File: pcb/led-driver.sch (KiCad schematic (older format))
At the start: 33 parts, among them Q201 Q_NMOS_GDSD, Q202 Q_NMOS_GDSD, Q203 Q_NMOS_GDSD, Q204 Q_NMOS_GDSD, Q205 NPN, Q206 NPN, Q207 NPN, Q208 NPN, U201 LM2902N, U202 MAX5813

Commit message: removed resistor dividors, added cap to usb
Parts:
- removed R205, R206, R207, R208, R209, R210, R211, R212: 10k, netl:SMD_0603, symbol R
- R213, R214, R215, R216, R217, R218, R219, R220: footprint (none) -> netl:SMD_0603
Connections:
- net A: now also U201.3 (+)
- net B: now also U201.5 (+)
- net C: now also U201.10 (+)
- net D: now also U201.12 (+)

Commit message: added mcu
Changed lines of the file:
@@
 $EndComp
 $Comp
-L GND #PWR026
+L GND #PWR022
 U 1 1 56C32C0C
 P 6350 4850
-F 0 "#PWR026" H 6350 4600 50  0001 C CNN
+F 0 "#PWR022" H 6350 4600 50  0001 C CNN
 F 1 "GND" H 6350 4700 50  0000 C CNN
 F 2 "" H 6350 4850 60  0000 C CNN
@@
 $EndComp
 $Comp
-L GND #PWR027
+L GND #PWR023
 U 1 1 56C32E31
 P 3200 4850
-F 0 "#PWR027" H 3200 4600 50  0001 C CNN
+F 0 "#PWR023" H 3200 4600 50  0001 C CNN
 F 1 "GND" H 3200 4700 50  0000 C CNN
 F 2 "" H 3200 4850 60  0000 C CNN
@@
 $EndComp
 $Comp
-L GND #PWR028
+L GND #PWR024
 U 1 1 56C32F90
 P 3200 2550
-F 0 "#PWR028" H 3200 2300 50  0001 C CNN
+F 0 "#PWR024" H 3200 2300 50  0001 C CNN
 F 1 "GND" H 3200 2400 50  0000 C CNN
 F 2 "" H 3200 2550 60  0000 C CNN
@@
 $EndComp
 $Comp
-L GND #PWR029
+L GND #PWR025
 U 1 1 56C33072
 P 6350 2550
-F 0 "#PWR029" H 6350 2300 50  0001 C CNN
+F 0 "#PWR025" H 6350 2300 50  0001 C CNN
 F 1 "GND" H 6350 2400 50  0000 C CNN
 F 2 "" H 6350 2550 60  0000 C CNN
@@
 	3550 2450 3550 2550
 Wire Wire Line
-	3550 1900 3550 2050
-Wire Wire Line
-	3550 2050 3550 2150
+	3550 1900 3550 2150
 Wire Wire Line
 	2200 1000 2200 1300
@@
 Connection ~ 6700 2050
 Wire Wire Line
-	6700 1900 6700 2050
-Wire Wire Line
-	6700 2050 6700 2150
+	6700 1900 6700 2150
 Wire Wire Line
 	4950 2050 4950 1800
@@
 	3950 6550 4050 6550
 Wire Wire Line
-	3800 6750 3950 6750
-Wire Wire Line
-	3950 6750 4050 6750
+	3800 6750 4050 6750
 Wire Wire Line
 	5150 6450 5000 6450
@@
 	5000 6750 5150 6750
 Wire Wire Line
-	5000 6150 5650 6150
-Wire Wire Line
-	5650 6150 5900 6150
-Wire Wire Line
-	5000 6150 5000 6250
-Wire Wire Line
-	5000 6250 5000 6350
+	5000 6150 5900 6150
+Wire Wire Line
+	5000 6150 5000 6350
 Connection ~ 5000 6250
 Wire Wire Line
@@
 	7750 2800 7750 2700
 Wire Wire Line
-	6700 4200 6700 4350
-Wire Wire Line
-	6700 4350 6700 4450
+	6700 4200 6700 4450
 Wire Wire Line
 	6700 3800 6800 3800
@@
 Connection ~ 6700 4350
 Wire Wire Line
-	3550 4200 3550 4350
-Wire Wire Line
-	3550 4350 3550 4450
+	3550 4200 3550 4450
 Connection ~ 3550 4350
 Wire Wire Line
@@
 	3550 1500 3650 1500
 Wire Wire Line
-	6300 1700 6350 1700
-Wire Wire Line
-	6350 1700 6400 1700
+	6300 1700 6400 1700
 Wire Wire Line
 	6700 1500 6800 1500
@@
 	5950 4000 6000 4000
 Wire Wire Line
-	6300 4000 6350 4000
-Wire Wire Line
-	6350 4000 6400 4000
+	6300 4000 6400 4000
 Wire Wire Line
 	6350 4400 6350 4000
@@
 	2800 1700 2850 1700
 Wire Wire Line
-	3150 1700 3200 1700
-Wire Wire Line
-	3200 1700 3250 1700
+	3150 1700 3250 1700
 Wire Wire Line
 	3200 2550 3200 2500
@@
 	3200 4400 3200 4000
 Wire Wire Line
-	3150 4000 3200 4000
-Wire Wire Line
-	3200 4000 3250 4000
+	3150 4000 3250 4000
 Connection ~ 3200 4000
 Wire Wire Line

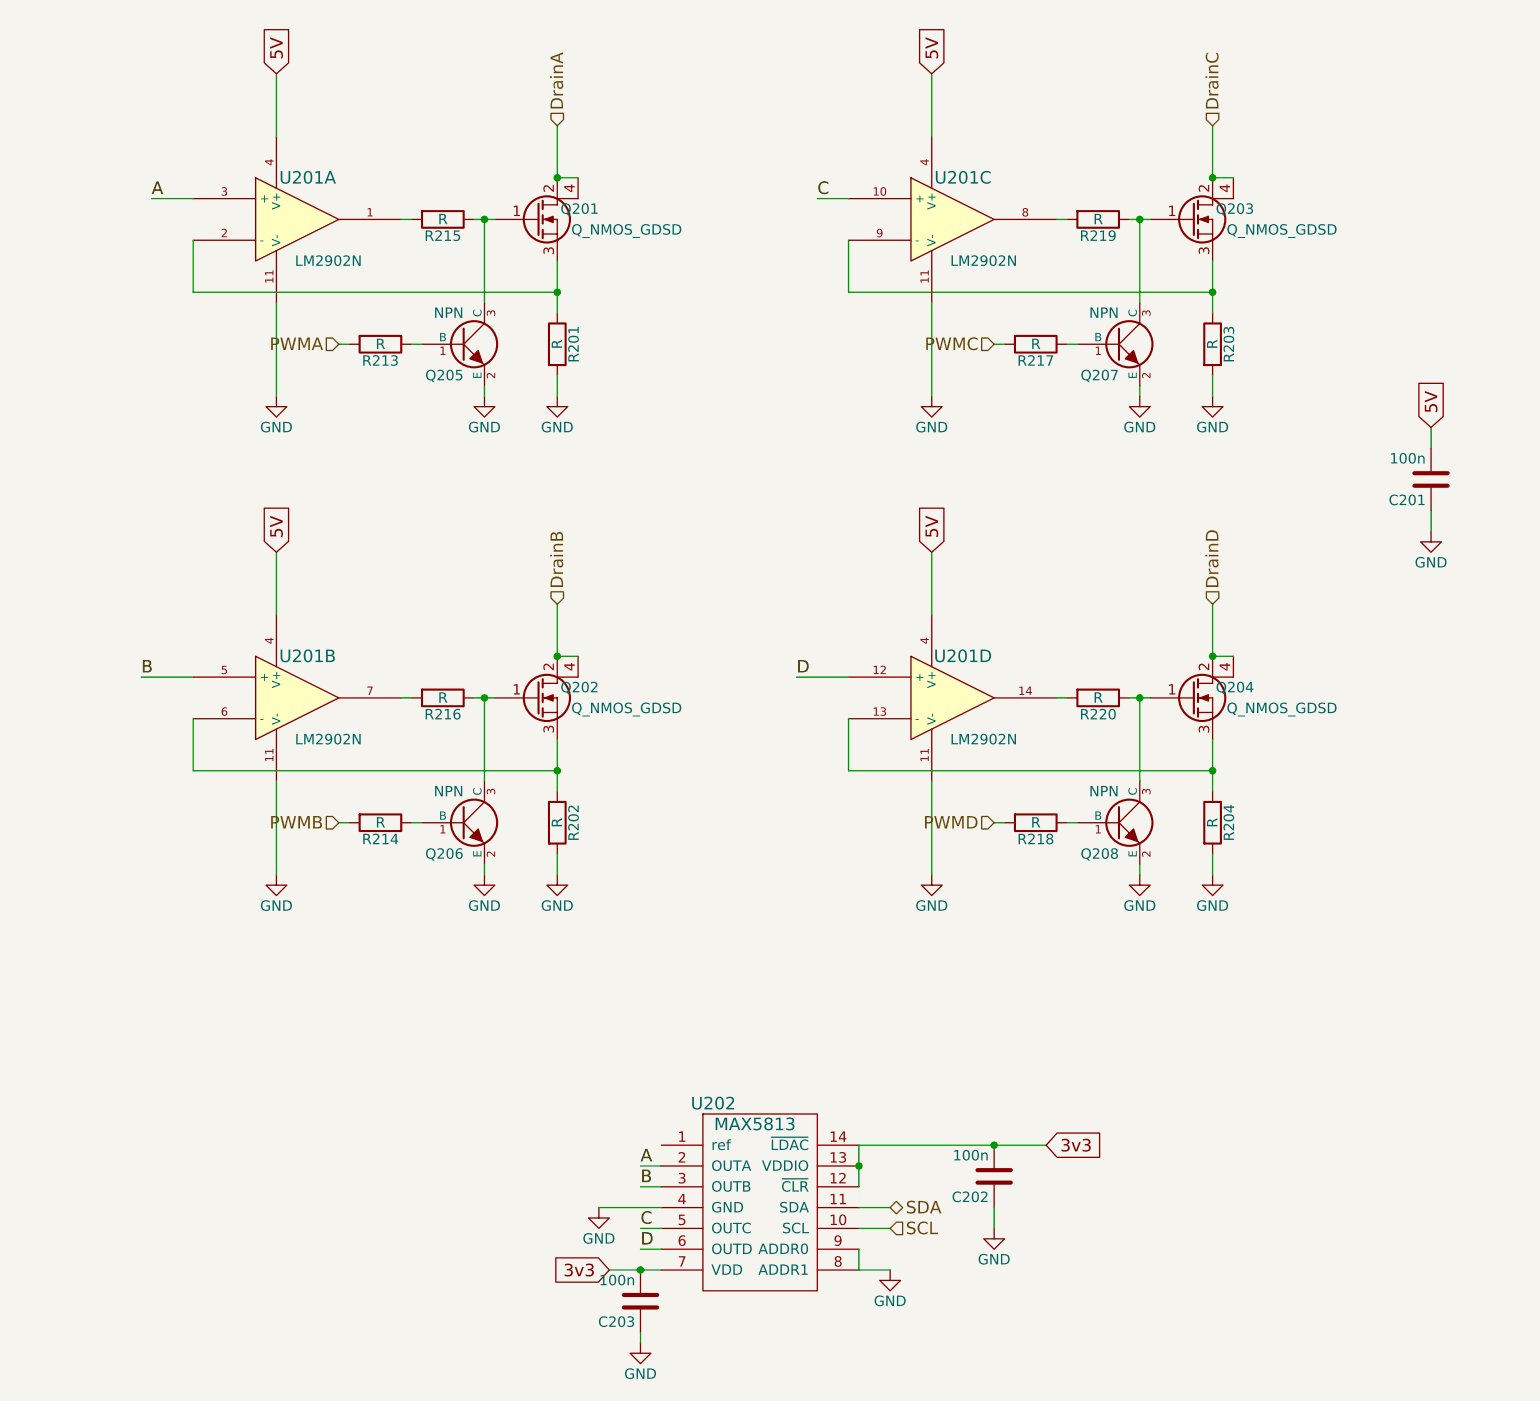
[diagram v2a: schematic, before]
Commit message: added the voltage dividers back to the constant-current control
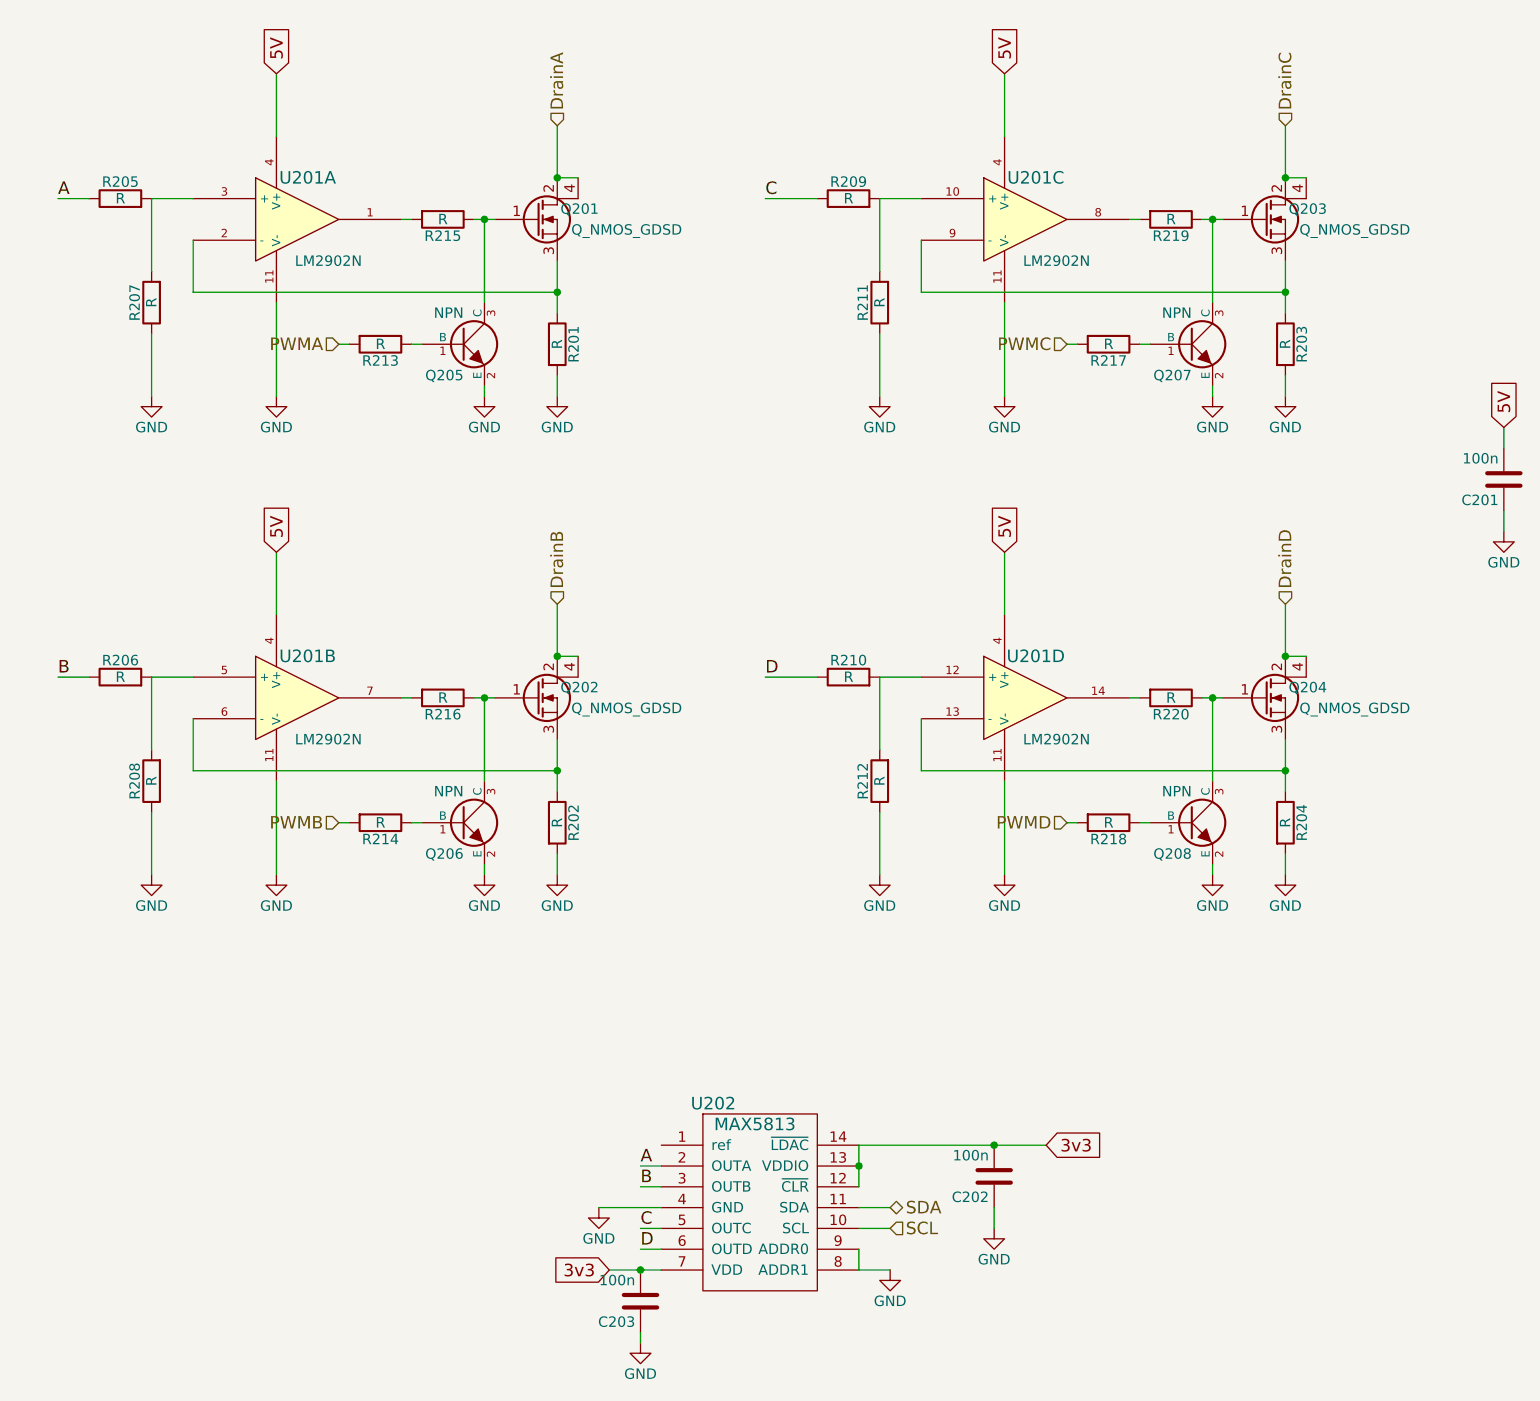
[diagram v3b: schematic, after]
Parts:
- added R205, R206, R207, R208, R209, R210, R211, R212: R, symbol R
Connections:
- net A: now also R205.1; no longer U201.3 (+)
- net B: now also R206.1; no longer U201.5 (+)
- net C: now also R209.1; no longer U201.10 (+)
- net D: now also R210.1; no longer U201.12 (+)
- net GND: now also R207.1, R208.1, R211.1, R212.1
- new net: R205.2, R207.2, U201.3 (+)
- new net: R210.2, R212.2, U201.12 (+)
- new net: R206.2, R208.2, U201.5 (+)
- new net: R209.2, R211.2, U201.10 (+)
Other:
- moved on the sheet: C201, Q203, Q204, Q207, Q208, R203, R204, R217, R218, R219, R220, U201C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

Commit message: added the damn resistors... again.
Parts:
- R205, R206, R207, R208, R209, R210, R211, R212: footprint (none) -> netl:SMD_0603
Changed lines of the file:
@@
 $EndDescr
 $Comp
-L GND #PWR207
+L GND #PWR09
 U 1 1 566DBED0
 P 3550 2550
-F 0 "#PWR207" H 3550 2300 50  0001 C CNN
+F 0 "#PWR09" H 3550 2300 50  0001 C CNN
 F 1 "GND" H 3550 2400 50  0000 C CNN
 F 2 "" H 3550 2550 60  0000 C CNN
@@
 $EndComp
 $Comp
-L GND #PWR203
+L GND #PWR010
 U 1 1 566DE548
 P 2200 2550
-F 0 "#PWR203" H 2200 2300 50  0001 C CNN
+F 0 "#PWR010" H 2200 2300 50  0001 C CNN
 F 1 "GND" H 2200 2400 50  0000 C CNN
 F 2 "" H 2200 2550 60  0000 C CNN
@@
 5V
 $Comp
-L GND #PWR208
+L GND #PWR011
 U 1 1 566E450E
 P 3550 4850
-F 0 "#PWR208" H 3550 4600 50  0001 C CNN
+F 0 "#PWR011" H 3550 4600 50  0001 C CNN
 F 1 "GND" H 3550 4700 50  0000 C CNN
 F 2 "" H 3550 4850 60  0000 C CNN
@@
 $EndComp
 $Comp
-L GND #PWR204
+L GND #PWR012
 U 1 1 566E453D
 P 2200 4850
-F 0 "#PWR204" H 2200 4600 50  0001 C CNN
+F 0 "#PWR012" H 2200 4600 50  0001 C CNN
 F 1 "GND" H 2200 4700 50  0000 C CNN
 F 2 "" H 2200 4850 60  0000 C CNN
@@
 $EndComp
 $Comp
-L GND #PWR219
+L GND #PWR013
 U 1 1 566E478C
 P 7050 2550
-F 0 "#PWR219" H 7050 2300 50  0001 C CNN
+F 0 "#PWR013" H 7050 2300 50  0001 C CNN
 F 1 "GND" H 7050 2400 50  0000 C CNN
 F 2 "" H 7050 2550 60  0000 C CNN
@@
 $EndComp
 $Comp
-L GND #PWR215
+L GND #PWR014
 U 1 1 566E47BB
 P 5700 2550
-F 0 "#PWR215" H 5700 2300 50  0001 C CNN
+F 0 "#PWR014" H 5700 2300 50  0001 C CNN
 F 1 "GND" H 5700 2400 50  0000 C CNN
 F 2 "" H 5700 2550 60  0000 C CNN
@@
 $EndComp
 $Comp
-L GND #PWR209
+L GND #PWR015
 U 1 1 566E84F5
 P 3750 6450
-F 0 "#PWR209" H 3750 6200 50  0001 C CNN
+F 0 "#PWR015" H 3750 6200 50  0001 C CNN
 F 1 "GND" H 3750 6300 50  0000 C CNN
 F 2 "" H 3750 6450 60  0000 C CNN
@@
 3v3
 $Comp
-L GND #PWR213
+L GND #PWR016
 U 1 1 566E8506
 P 5150 6750
-F 0 "#PWR213" H 5150 6500 50  0001 C CNN
+F 0 "#PWR016" H 5150 6500 50  0001 C CNN
 F 1 "GND" H 5150 6600 50  0000 C CNN
 F 2 "" H 5150 6750 60  0000 C CNN
@@
 SCL
 $Comp
-L GND #PWR220
+L GND #PWR017
 U 1 1 566E01A5
 P 7050 4850
-F 0 "#PWR220" H 7050 4600 50  0001 C CNN
+F 0 "#PWR017" H 7050 4600 50  0001 C CNN
 F 1 "GND" H 7050 4700 50  0000 C CNN
 F 2 "" H 7050 4850 60  0000 C CNN
@@
 $EndComp
 $Comp
-L GND #PWR216
+L GND #PWR018
 U 1 1 566E01CE
 P 5700 4850
-F 0 "#PWR216" H 5700 4600 50  0001 C CNN
+F 0 "#PWR018" H 5700 4600 50  0001 C CNN
 F 1 "GND" H 5700 4700 50  0000 C CNN
 F 2 "" H 5700 4850 60  0000 C CNN
@@
 5V
 $Comp
-L GND #PWR221
+L GND #PWR019
 U 1 1 566EAF9B
 P 8100 3200
-F 0 "#PWR221" H 8100 2950 50  0001 C CNN
+F 0 "#PWR019" H 8100 2950 50  0001 C CNN
 F 1 "GND" H 8100 3050 50  0000 C CNN
 F 2 "" H 8100 3200 60  0000 C CNN
@@
 $EndComp
 $Comp
-L GND #PWR214
+L GND #PWR020
 U 1 1 56B92263
 P 5650 6550
-F 0 "#PWR214" H 5650 6300 50  0001 C CNN
+F 0 "#PWR020" H 5650 6300 50  0001 C CNN
 F 1 "GND" H 5650 6400 50  0000 C CNN
 F 2 "" H 5650 6550 60  0000 C CNN
@@
 $EndComp
 $Comp
-L GND #PWR210
+L GND #PWR021
 U 1 1 56B92D0C
 P 3950 7100
-F 0 "#PWR210" H 3950 6850 50  0001 C CNN
+F 0 "#PWR021" H 3950 6850 50  0001 C CNN
 F 1 "GND" H 3950 6950 50  0000 C CNN
 F 2 "" H 3950 7100 60  0000 C CNN
@@
 $EndComp
 $Comp
-L GND #PWR218
+L GND #PWR022
 U 1 1 56C32C0C
 P 6700 4850
-F 0 "#PWR218" H 6700 4600 50  0001 C CNN
+F 0 "#PWR022" H 6700 4600 50  0001 C CNN
 F 1 "GND" H 6700 4700 50  0000 C CNN
 F 2 "" H 6700 4850 60  0000 C CNN
@@
 $EndComp
 $Comp
-L GND #PWR206
+L GND #PWR023
 U 1 1 56C32E31
 P 3200 4850
-F 0 "#PWR206" H 3200 4600 50  0001 C CNN
+F 0 "#PWR023" H 3200 4600 50  0001 C CNN
 F 1 "GND" H 3200 4700 50  0000 C CNN
 F 2 "" H 3200 4850 60  0000 C CNN
@@
 $EndComp
 $Comp
-L GND #PWR205
+L GND #PWR024
 U 1 1 56C32F90
 P 3200 2550
-F 0 "#PWR205" H 3200 2300 50  0001 C CNN
+F 0 "#PWR024" H 3200 2300 50  0001 C CNN
 F 1 "GND" H 3200 2400 50  0000 C CNN
 F 2 "" H 3200 2550 60  0000 C CNN
@@
 $EndComp
 $Comp
-L GND #PWR217
+L GND #PWR025
 U 1 1 56C33072
 P 6700 2550
-F 0 "#PWR217" H 6700 2300 50  0001 C CNN
+F 0 "#PWR025" H 6700 2300 50  0001 C CNN
 F 1 "GND" H 6700 2400 50  0000 C CNN
 F 2 "" H 6700 2550 60  0000 C CNN
@@
 F 0 "R210" V 5030 3900 50  0000 C CNN
 F 1 "R" V 4950 3900 50  0000 C CNN
-F 2 "" V 4880 3900 50  0000 C CNN
+F 2 "netl:SMD_0603" V 4880 3900 50  0001 C CNN
 F 3 "" H 4950 3900 50  0000 C CNN
 	1    4950 3900
@@
 F 0 "R212" V 5180 4400 50  0000 C CNN
 F 1 "R" V 5100 4400 50  0000 C CNN
-F 2 "" V 5030 4400 50  0000 C CNN
+F 2 "netl:SMD_0603" V 5030 4400 50  0001 C CNN
 F 3 "" H 5100 4400 50  0000 C CNN
 	1    5100 4400
@@
 $EndComp
 $Comp
-L GND #PWR212
+L GND #PWR026
 U 1 1 578B9C66
 P 5100 4850
-F 0 "#PWR212" H 5100 4600 50  0001 C CNN
+F 0 "#PWR026" H 5100 4600 50  0001 C CNN
 F 1 "GND" H 5100 4700 50  0000 C CNN
 F 2 "" H 5100 4850 60  0000 C CNN
@@
 	3550 2450 3550 2550
 Wire Wire Line
-	3550 1900 3550 2050
-Wire Wire Line
-	3550 2050 3550 2150
+	3550 1900 3550 2150
 Wire Wire Line
 	2200 1000 2200 1300
@@
 Connection ~ 7050 2050
 Wire Wire Line
-	7050 1900 7050 2050
-Wire Wire Line
-	7050 2050 7050 2150
+	7050 1900 7050 2150
 Wire Wire Line
 	5300 2050 5300 1800
@@
 	3950 6550 4050 6550
 Wire Wire Line
-	3800 6750 3950 6750
-Wire Wire Line
-	3950 6750 4050 6750
+	3800 6750 4050 6750
 Wire Wire Line
 	5150 6450 5000 6450
@@
 	5000 6750 5150 6750
 Wire Wire Line
-	5000 6150 5650 6150
-Wire Wire Line
-	5650 6150 5900 6150
-Wire Wire Line
-	5000 6150 5000 6250
-Wire Wire Line
-	5000 6250 5000 6350
+	5000 6150 5900 6150
+Wire Wire Line
+	5000 6150 5000 6350
 Connection ~ 5000 6250
 Wire Wire Line
@@
 	8100 2800 8100 2700
 Wire Wire Line
-	7050 4200 7050 4350
-Wire Wire Line
-	7050 4350 7050 4450
+	7050 4200 7050 4450
 Wire Wire Line
 	7050 3800 7150 3800
@@
 Connection ~ 7050 4350
 Wire Wire Line
-	3550 4200 3550 4350
-Wire Wire Line
-	3550 4350 3550 4450
+	3550 4200 3550 4450
 Connection ~ 3550 4350
 Wire Wire Line
@@
 	3550 1500 3650 1500
 Wire Wire Line
-	6650 1700 6700 1700
-Wire Wire Line
-	6700 1700 6750 1700
+	6650 1700 6750 1700
 Wire Wire Line
 	7050 1500 7150 1500
@@
 	6300 4000 6350 4000
 Wire Wire Line
-	6650 4000 6700 4000
-Wire Wire Line
-	6700 4000 6750 4000
+	6650 4000 6750 4000
 Wire Wire Line
 	6700 4400 6700 4000
@@
 	2800 1700 2850 1700
 Wire Wire Line
-	3150 1700 3200 1700
-Wire Wire Line
-	3200 1700 3250 1700
+	3150 1700 3250 1700
 Wire Wire Line
 	3200 2550 3200 2500
@@
 	3200 4400 3200 4000
 Wire Wire Line
-	3150 4000 3200 4000
-Wire Wire Line
-	3200 4000 3250 4000
+	3150 4000 3250 4000
 Connection ~ 3200 4000
 Wire Wire Line
@@
 F 0 "R209" V 5030 1600 50  0000 C CNN
 F 1 "R" V 4950 1600 50  0000 C CNN
-F 2 "" V 4880 1600 50  0000 C CNN
+F 2 "netl:SMD_0603" V 4880 1600 50  0001 C CNN
 F 3 "" H 4950 1600 50  0000 C CNN
 	1    4950 1600
@@
 F 0 "R211" V 5180 2100 50  0000 C CNN
 F 1 "R" V 5100 2100 50  0000 C CNN
-F 2 "" V 5030 2100 50  0000 C CNN
+F 2 "netl:SMD_0603" V 5030 2100 50  0001 C CNN
 F 3 "" H 5100 2100 50  0000 C CNN
 	1    5100 2100
@@
 $EndComp
 $Comp
-L GND #PWR211
+L GND #PWR027
 U 1 1 578BAABF
 P 5100 2550
-F 0 "#PWR211" H 5100 2300 50  0001 C CNN
+F 0 "#PWR027" H 5100 2300 50  0001 C CNN
 F 1 "GND" H 5100 2400 50  0000 C CNN
 F 2 "" H 5100 2550 60  0000 C CNN
@@
 F 0 "R205" V 1530 1600 50  0000 C CNN
 F 1 "R" V 1450 1600 50  0000 C CNN
-F 2 "" V 1380 1600 50  0000 C CNN
+F 2 "netl:SMD_0603" V 1380 1600 50  0001 C CNN
 F 3 "" H 1450 1600 50  0000 C CNN
 	1    1450 1600
@@
 F 0 "R207" V 1680 2100 50  0000 C CNN
 F 1 "R" V 1600 2100 50  0000 C CNN
-F 2 "" V 1530 2100 50  0000 C CNN
+F 2 "netl:SMD_0603" V 1530 2100 50  0001 C CNN
 F 3 "" H 1600 2100 50  0000 C CNN
 	1    1600 2100
@@
 $EndComp
 $Comp
-L GND #PWR201
+L GND #PWR028
 U 1 1 578BB092
 P 1600 2550
-F 0 "#PWR201" H 1600 2300 50  0001 C CNN
+F 0 "#PWR028" H 1600 2300 50  0001 C CNN
 F 1 "GND" H 1600 2400 50  0000 C CNN
 F 2 "" H 1600 2550 60  0000 C CNN
@@
 F 0 "R206" V 1530 3900 50  0000 C CNN
 F 1 "R" V 1450 3900 50  0000 C CNN
-F 2 "" V 1380 3900 50  0000 C CNN
+F 2 "netl:SMD_0603" V 1380 3900 50  0001 C CNN
 F 3 "" H 1450 3900 50  0000 C CNN
 	1    1450 3900
@@
 F 0 "R208" V 1680 4400 50  0000 C CNN
 F 1 "R" V 1600 4400 50  0000 C CNN
-F 2 "" V 1530 4400 50  0000 C CNN
+F 2 "netl:SMD_0603" V 1530 4400 50  0001 C CNN
 F 3 "" H 1600 4400 50  0000 C CNN
 	1    1600 4400
@@
 $EndComp
 $Comp
-L GND #PWR202
+L GND #PWR029
 U 1 1 578BB867
 P 1600 4850
-F 0 "#PWR202" H 1600 4600 50  0001 C CNN
+F 0 "#PWR029" H 1600 4600 50  0001 C CNN
 F 1 "GND" H 1600 4700 50  0000 C CNN
 F 2 "" H 1600 4850 60  0000 C CNN

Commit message: working version from assembly 2016
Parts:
- R205, R206, R209, R210: value R -> 10k
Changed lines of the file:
@@
 LIBS:contrib
 LIBS:valves
-LIBS:netl
 LIBS:rpi_shield-cache
 EELAYER 25 0
@@
 P 4950 3900
 F 0 "R210" V 5030 3900 50  0000 C CNN
-F 1 "R" V 4950 3900 50  0000 C CNN
+F 1 "10k" V 4950 3900 50  0000 C CNN
 F 2 "netl:SMD_0603" V 4880 3900 50  0001 C CNN
 F 3 "" H 4950 3900 50  0000 C CNN
@@
 P 4950 1600
 F 0 "R209" V 5030 1600 50  0000 C CNN
-F 1 "R" V 4950 1600 50  0000 C CNN
+F 1 "10k" V 4950 1600 50  0000 C CNN
 F 2 "netl:SMD_0603" V 4880 1600 50  0001 C CNN
 F 3 "" H 4950 1600 50  0000 C CNN
@@
 P 1450 1600
 F 0 "R205" V 1530 1600 50  0000 C CNN
-F 1 "R" V 1450 1600 50  0000 C CNN
+F 1 "10k" V 1450 1600 50  0000 C CNN
 F 2 "netl:SMD_0603" V 1380 1600 50  0001 C CNN
 F 3 "" H 1450 1600 50  0000 C CNN
@@
 P 1450 3900
 F 0 "R206" V 1530 3900 50  0000 C CNN
-F 1 "R" V 1450 3900 50  0000 C CNN
+F 1 "10k" V 1450 3900 50  0000 C CNN
 F 2 "netl:SMD_0603" V 1380 3900 50  0001 C CNN
 F 3 "" H 1450 3900 50  0000 C CNN
